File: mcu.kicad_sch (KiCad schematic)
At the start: 25 parts, among them J2 Conn_01x06_GH1.25, SW1 RST, U5 XC6206PxxxMR, U7 AT32F425K8U7-4, U8 TJA1044GTK/3Z, Y1 16MHz

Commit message: 暂存: 基本完成原理图(未分配封装，未ERC)
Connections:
- net CANH: no longer U8.7 (CANH)
- net CANL: no longer U8.6 (CANL)
- net CANH_IN: now reaches D10.1, R11.2, R9.1
- net CANH_IN: now also U8.7 (CANH)
- net CANL_IN: now reaches D10.2, R10.2, R12.2
- net CANL_IN: now also U8.6 (CANL)
- net 5V0 renamed 5V0_{assist}
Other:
- note removed: "差CAN接头"
- moved on the sheet: C60, D10, J2, R10, R11, R12, R9, U7, U8

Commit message: 暂存: 基本完成原理图(差雷达接口)
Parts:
- C1: renamed from C23; footprint Capacitor_SMD:C_0603_1608Metric -> Capacitor_SMD:C_0402_1005Metric
- C11: renamed from C60; footprint (none) -> Capacitor_SMD:C_0402_1005Metric
- C8: renamed from C30; footprint Capacitor_SMD:C_0603_1608Metric -> Capacitor_SMD:C_0402_1005Metric
- R3: renamed from R11; footprint (none) -> Resistor_SMD:R_0402_1005Metric
- R4: renamed from R12; footprint (none) -> Resistor_SMD:R_0402_1005Metric
- R5: renamed from R9; footprint (none) -> Resistor_SMD:R_0402_1005Metric
- R6: renamed from R10; footprint (none) -> Resistor_SMD:R_0402_1005Metric
- renumbered C32 to C10, C24 to C2, C25 to C3, C26 to C4, C27 to C5, C28 to C6, C29 to C7, C31 to C9, D10 to D1, J2 to J1, R15 to R1, R16 to R2, TP3 to TP1, U5 to U1, U7 to U2, U8 to U3
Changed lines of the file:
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@@
 		(dnp no)
 		(fields_autoplaced yes)
-		(property "Reference" "R9"
+		(property "Reference" "R5"
 			(at 161.29 59.6899 0)
 			(effects
@@
 			)
 		)
-		(property "Footprint" ""
+		(property "Footprint" "Resistor_SMD:R_0402_1005Metric"
 			(at 158.75 60.96 0)
 			(effects
@@
 			(project ""
 				(path "/c658c753-a869-4eb9-a520-6b2e7fae7fd9/bed308e1-7b03-4f89-9efc-3e92ee91bd02"
-					(reference "R9")
+					(reference "R5")
 					(unit 1)
 				)
@@
 		(dnp no)
 		(fields_autoplaced yes)
-		(property "Reference" "U7"
+		(property "Reference" "U2"
 			(at 106.68 66.04 0)
 			(effects
@@
 			(project ""
 				(path "/c658c753-a869-4eb9-a520-6b2e7fae7fd9/bed308e1-7b03-4f89-9efc-3e92ee91bd02"
-					(reference "U7")
+					(reference "U2")
 					(unit 1)
 				)
@@
 		(dnp no)
 		(fields_autoplaced yes)
-		(property "Reference" "#PWR6"
+		(property "Reference" "#PWR1"
 			(at 172.72 81.28 0)
 			(effects
@@
 			(project ""
 				(path "/c658c753-a869-4eb9-a520-6b2e7fae7fd9/bed308e1-7b03-4f89-9efc-3e92ee91bd02"
-					(reference "#PWR6")
+					(reference "#PWR1")
 					(unit 1)
 				)
@@
 		(on_board yes)
 		(dnp no)
-		(property "Reference" "TP3"
+		(property "Reference" "TP1"
 			(at 75.184 30.988 0)
 			(effects
@@
 			(project "ZW1S"
 				(path "/c658c753-a869-4eb9-a520-6b2e7fae7fd9/bed308e1-7b03-4f89-9efc-3e92ee91bd02"
-					(reference "TP3")
+					(reference "TP1")
 					(unit 1)
 				)
@@
 		(dnp no)
 		(fields_autoplaced yes)
-		(property "Reference" "C23"
+		(property "Reference" "C1"
 			(at 40.64 36.8362 0)
 			(effects
@@
 			)
 		)
-		(property "Footprint" "Capacitor_SMD:C_0603_1608Metric"
+		(property "Footprint" "Capacitor_SMD:C_0402_1005Metric"
 			(at 38.1 38.1 0)
 			(effects
@@
 			(project "ZW1S"
 				(path "/c658c753-a869-4eb9-a520-6b2e7fae7fd9/bed308e1-7b03-4f89-9efc-3e92ee91bd02"
-					(reference "C23")
+					(reference "C1")
 					(unit 1)
 				)
@@
 		(dnp no)
 		(fields_autoplaced yes)
-		(property "Reference" "R12"
+		(property "Reference" "R4"
 			(at 153.67 67.31 90)
 			(effects
@@
 			)
 		)
-		(property "Footprint" ""
+		(property "Footprint" "Resistor_SMD:R_0402_1005Metric"
 			(at 153.67 72.39 0)
 			(effects
@@
 			(project "ZW1S"
 				(path "/c658c753-a869-4eb9-a520-6b2e7fae7fd9/bed308e1-7b03-4f89-9efc-3e92ee91bd02"
-					(reference "R12")
+					(reference "R4")
 					(unit 1)
 				)
@@
 		(on_board yes)
 		(dnp no)
-		(property "Reference" "C25"
+		(property "Reference" "C3"
 			(at 39.37 120.65 90)
 			(effects
@@
 			(project "ZW1S"
 				(path "/c658c753-a869-4eb9-a520-6b2e7fae7fd9/bed308e1-7b03-4f89-9efc-3e92ee91bd02"
-					(reference "C25")
+					(reference "C3")
 					(unit 1)
 				)
@@
 		(on_board yes)
 		(dnp no)
-		(property "Reference" "R16"
+		(property "Reference" "R2"
 			(at 40.132 59.69 90)
 			(effects
@@
 			(project "ZW1S"
 				(path "/c658c753-a869-4eb9-a520-6b2e7fae7fd9/bed308e1-7b03-4f89-9efc-3e92ee91bd02"
-					(reference "R16")
+					(reference "R2")
 					(unit 1)
 				)
@@
 		(on_board yes)
 		(dnp no)
-		(property "Reference" "C28"
+		(property "Reference" "C6"
 			(at 38.1 134.62 90)
 			(effects
@@
 			(project "ZW1S"
 				(path "/c658c753-a869-4eb9-a520-6b2e7fae7fd9/bed308e1-7b03-4f89-9efc-3e92ee91bd02"
-					(reference "C28")
+					(reference "C6")
 					(unit 1)
 				)
@@
 		(dnp no)
 		(fields_autoplaced yes)
-		(property "Reference" "D10"
+		(property "Reference" "D1"
 			(at 181.61 55.88 0)
 			(effects
@@
 			(project ""
 				(path "/c658c753-a869-4eb9-a520-6b2e7fae7fd9/bed308e1-7b03-4f89-9efc-3e92ee91bd02"
-					(reference "D10")
+					(reference "D1")
 					(unit 1)
 				)
@@
 		(on_board yes)
 		(dnp no)
-		(property "Reference" "C27"
+		(property "Reference" "C5"
 			(at 38.1 130.81 90)
 			(effects
@@
 			(project "ZW1S"
 				(path "/c658c753-a869-4eb9-a520-6b2e7fae7fd9/bed308e1-7b03-4f89-9efc-3e92ee91bd02"
-					(reference "C27")
+					(reference "C5")
 					(unit 1)
 				)
@@
 		(on_board yes)
 		(dnp no)
-		(property "Reference" "J2"
+		(property "Reference" "J1"
 			(at 153.924 113.538 0)
 			(effects
@@
 			(project "ZW1S"
 				(path "/c658c753-a869-4eb9-a520-6b2e7fae7fd9/bed308e1-7b03-4f89-9efc-3e92ee91bd02"
-					(reference "J2")
+					(reference "J1")
 					(unit 1)
 				)
@@
 		(on_board yes)
 		(dnp yes)
-		(property "Reference" "C60"
+		(property "Reference" "C11"
 			(at 167.894 61.722 90)
 			(effects
@@
 			)
 		)
-		(property "Footprint" ""
+		(property "Footprint" "Capacitor_SMD:C_0402_1005Metric"
 			(at 168.91 64.77 0)
 			(effects
@@
 			(project ""
 				(path "/c658c753-a869-4eb9-a520-6b2e7fae7fd9/bed308e1-7b03-4f89-9efc-3e92ee91bd02"
-					(reference "C60")
+					(reference "C11")
 					(unit 1)
 				)
@@
 		(on_board yes)
 		(dnp no)
-		(property "Reference" "C30"
+		(property "Reference" "C8"
 			(at 67.31 36.8362 0)
 			(effects
@@
 			)
 		)
-		(property "Footprint" "Capacitor_SMD:C_0603_1608Metric"
+		(property "Footprint" "Capacitor_SMD:C_0402_1005Metric"
 			(at 69.85 38.1 0)
 			(effects
@@
 			(project "ZW1S"
 				(path "/c658c753-a869-4eb9-a520-6b2e7fae7fd9/bed308e1-7b03-4f89-9efc-3e92ee91bd02"
-					(reference "C30")
+					(reference "C8")
 					(unit 1)
 				)
@@
 		(on_board yes)
 		(dnp no)
-		(property "Reference" "U5"
+		(property "Reference" "U1"
 			(at 44.958 29.21 0)
 			(effects
@@
 			(project "ZW1S"
 				(path "/c658c753-a869-4eb9-a520-6b2e7fae7fd9/bed308e1-7b03-4f89-9efc-3e92ee91bd02"
-					(reference "U5")
+					(reference "U1")
 					(unit 1)
 				)
@@
 		(on_board yes)
 		(dnp yes)
-		(property "Reference" "R15"
+		(property "Reference" "R1"
 			(at 40.132 53.34 90)
 			(effects
@@
 			(project "ZW1S"
 				(path "/c658c753-a869-4eb9-a520-6b2e7fae7fd9/bed308e1-7b03-4f89-9efc-3e92ee91bd02"
-					(reference "R15")
+					(reference "R1")
 					(unit 1)
 				)
@@
 		(dnp no)
 		(fields_autoplaced yes)
-		(property "Reference" "C31"
+		(property "Reference" "C9"
 			(at 104.1463 27.94 90)
 			(effects
@@
 			(project "ZW1S"
 				(path "/c658c753-a869-4eb9-a520-6b2e7fae7fd9/bed308e1-7b03-4f89-9efc-3e92ee91bd02"
-					(reference "C31")
+					(reference "C9")
 					(unit 1)
 				)
@@
 		(dnp no)
 		(fields_autoplaced yes)
-		(property "Reference" "C32"
+		(property "Reference" "C10"
 			(at 104.1463 33.02 90)
 			(effects
@@
 			(project "ZW1S"
 				(path "/c658c753-a869-4eb9-a520-6b2e7fae7fd9/bed308e1-7b03-4f89-9efc-3e92ee91bd02"
-					(reference "C32")
+					(reference "C10")
 					(unit 1)
 				)
@@
 		(dnp no)
 		(fields_autoplaced yes)
-		(property "Reference" "C29"
+		(property "Reference" "C7"
 			(at 46.99 78.1113 0)
 			(effects
@@
 			(project "ZW1S"
 				(path "/c658c753-a869-4eb9-a520-6b2e7fae7fd9/bed308e1-7b03-4f89-9efc-3e92ee91bd02"
-					(reference "C29")
+					(reference "C7")
 					(unit 1)
 				)
@@
 		(on_board yes)
 		(dnp no)
-		(property "Reference" "C24"
+		(property "Reference" "C2"
 			(at 38.1 113.03 90)
 			(effects
@@
 			(project "ZW1S"
 				(path "/c658c753-a869-4eb9-a520-6b2e7fae7fd9/bed308e1-7b03-4f89-9efc-3e92ee91bd02"
-					(reference "C24")
+					(reference "C2")
 					(unit 1)
 				)
@@
 		(dnp no)
 		(fields_autoplaced yes)
-		(property "Reference" "U8"
+		(property "Reference" "U3"
 			(at 166.37 27.94 0)
 			(effects
@@
 			(project ""
 				(path "/c658c753-a869-4eb9-a520-6b2e7fae7fd9/bed308e1-7b03-4f89-9efc-3e92ee91bd02"
-					(reference "U8")
+					(reference "U3")
 					(unit 1)
 				)
@@
 		(dnp no)
 		(fields_autoplaced yes)
-		(property "Reference" "R10"
+		(property "Reference" "R6"
 			(at 161.29 67.3099 0)
 			(effects
@@
 			)
 		)
-		(property "Footprint" ""
+		(property "Footprint" "Resistor_SMD:R_0402_1005Metric"
 			(at 158.75 68.58 0)
 			(effects
@@
 			(project "ZW1S"
 				(path "/c658c753-a869-4eb9-a520-6b2e7fae7fd9/bed308e1-7b03-4f89-9efc-3e92ee91bd02"
-					(reference "R10")
+					(reference "R6")
 					(unit 1)
 				)
@@
 		(on_board yes)
 		(dnp no)
-		(property "Reference" "C26"
+		(property "Reference" "C4"
 			(at 38.1 127 90)
 			(effects
@@
 			(project "ZW1S"
 				(path "/c658c753-a869-4eb9-a520-6b2e7fae7fd9/bed308e1-7b03-4f89-9efc-3e92ee91bd02"
-					(reference "C26")
+					(reference "C4")
 					(unit 1)
 				)
@@
 		(dnp no)
 		(fields_autoplaced yes)
-		(property "Reference" "R11"
+		(property "Reference" "R3"
 			(at 153.67 52.07 90)
 			(effects
@@
 			)
 		)
-		(property "Footprint" ""
+		(property "Footprint" "Resistor_SMD:R_0402_1005Metric"
 			(at 153.67 57.15 0)
 			(effects
@@
 			(project "ZW1S"
 				(path "/c658c753-a869-4eb9-a520-6b2e7fae7fd9/bed308e1-7b03-4f89-9efc-3e92ee91bd02"
-					(reference "R11")
-					(unit 1)
-				)
+					(reference "R3")
+					(unit 1)
+				)

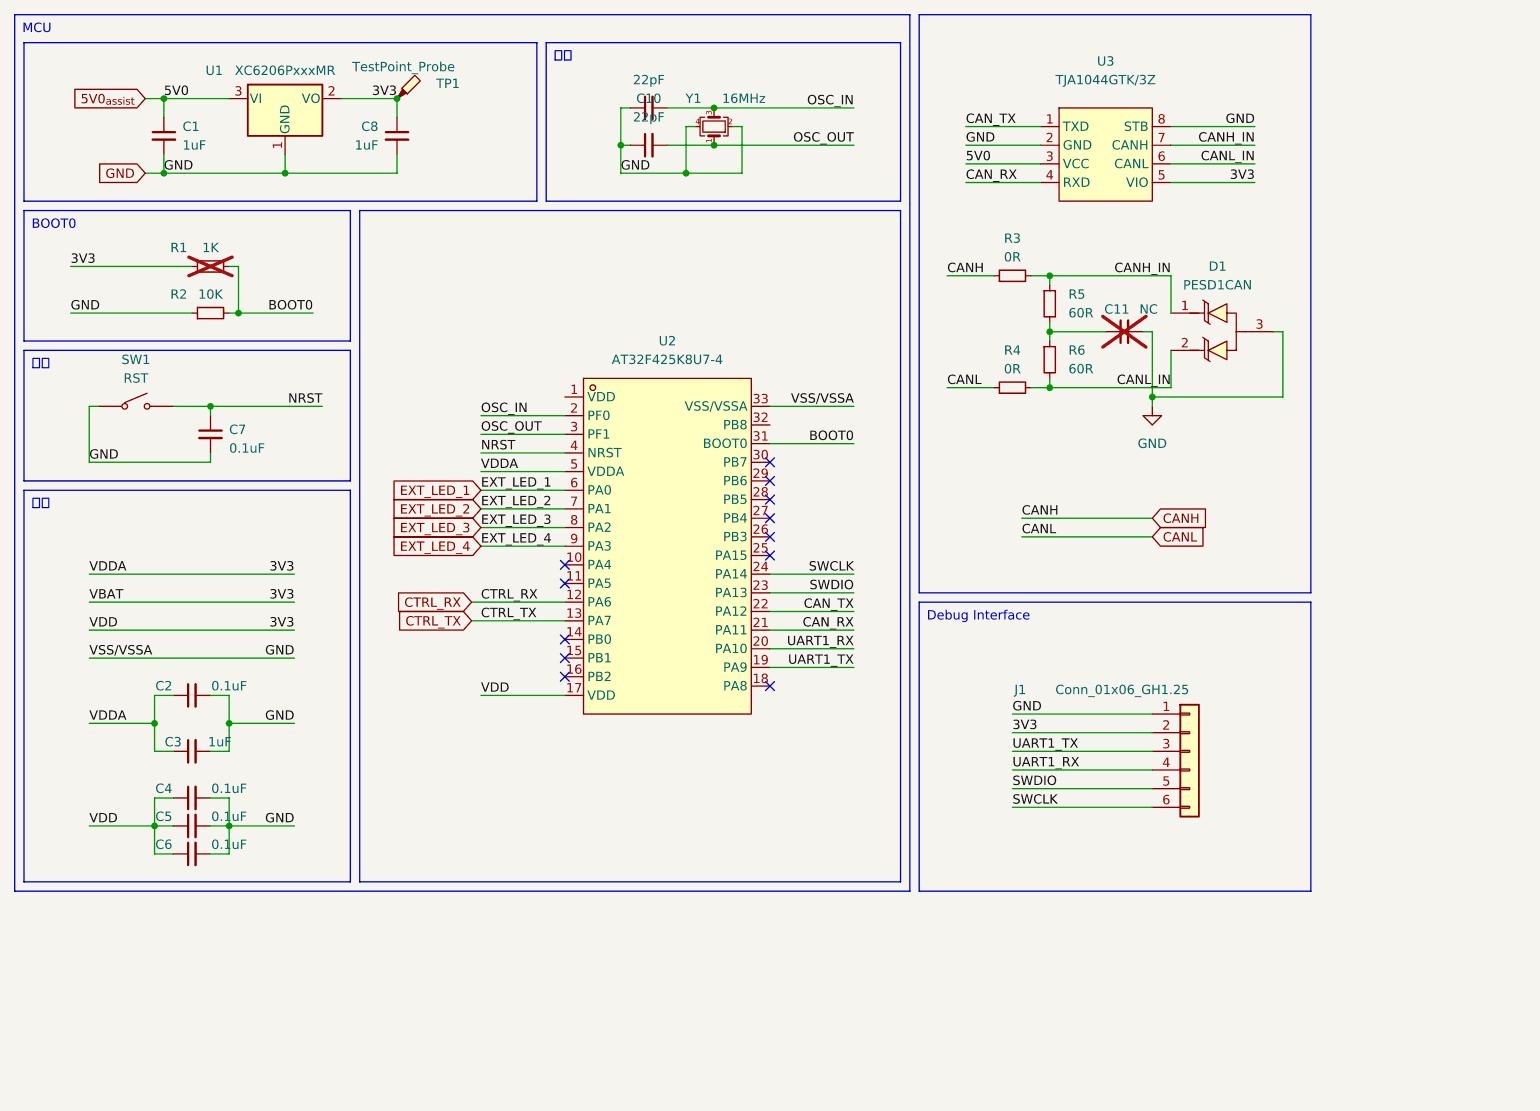
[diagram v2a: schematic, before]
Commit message: 暂存: 布局布线基本完成(DRC未过，GND不全)
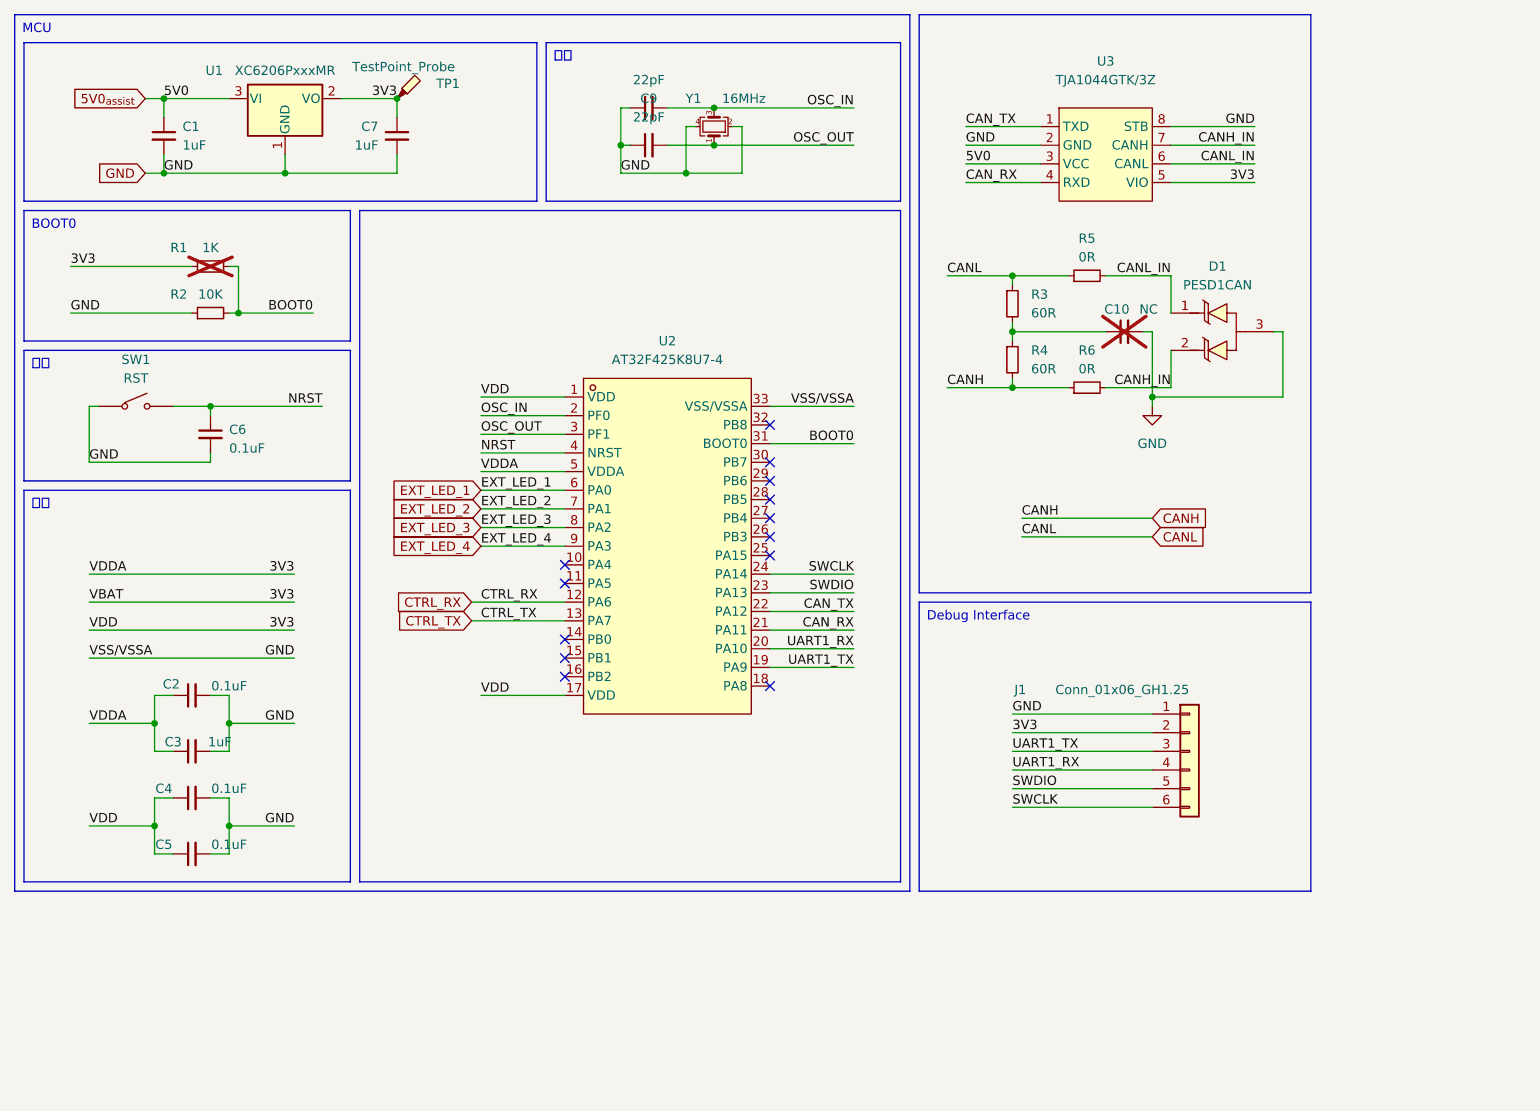
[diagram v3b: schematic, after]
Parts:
- removed C5: 0.1uF, Capacitor_SMD:C_0402_1005Metric, symbol Device:C_Small
- renumbered C11 to C10, C6 to C5, C7 to C6, C8 to C7, C9 to C8, C10 to C9, R5 to R3, R6 to R4, R3 to R5, R4 to R6
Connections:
- net 3V3: now also U2.1 (VDD)
- net CANH: now also R4.2, R6.1; no longer R5.1
- net CANH_IN: now also D1.2, R6.2; no longer D1.1, R3.1, R5.2
- net CANL: now also R3.1, R5.1; no longer R6.1
- net CANL_IN: now also D1.1, R5.2; no longer D1.2, R4.2, R6.2
- no-connect marks 12 -> 13
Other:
- moved on the sheet: R3, R4, R5, R6

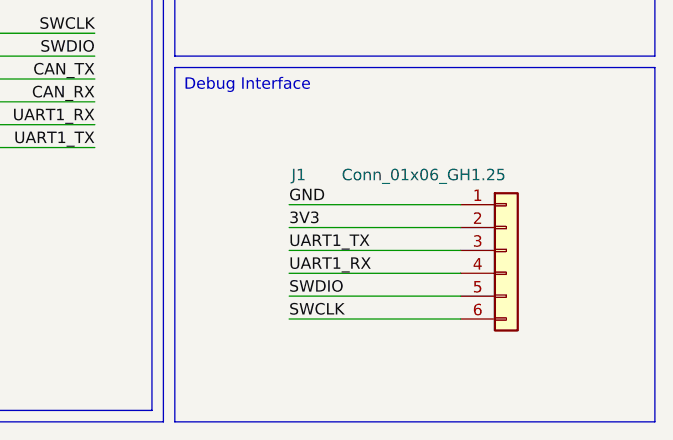
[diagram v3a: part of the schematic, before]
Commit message: pref: USB外设改自供电，优化布线
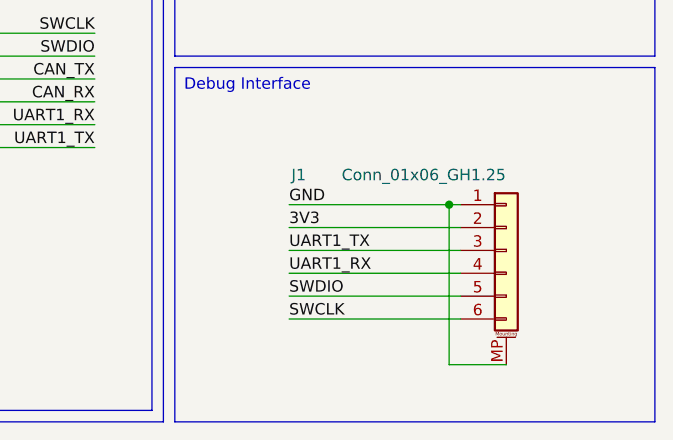
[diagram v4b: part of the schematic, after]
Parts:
- J1: footprint Connector_JST:JST_GH_BM06B-GHS-TBT_1x06-1MP_P1.25mm_Vertical -> Connector_JST:JST_GH_SM06B-GHS-TB_1x06-1MP_P1.25mm_Horizontal; symbol Connector_Generic:Conn_01x06 -> Connector_Generic_MountingPin:Conn_01x06_MountingPin
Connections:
- net EP: now also J1.MP (MountPin)
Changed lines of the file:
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@@
+		(color 0 0 0 0)
+	)
+	(junction
+		(at 171.45 116.84)
+		(diameter 0)
 		(color 0 0 0 0)
 	)
@@
 	(wire
 		(pts
+			(xy 171.45 116.84) (xy 172.72 116.84)
+		)
+		(stroke
+			(width 0)
+			(type default)
+		)
+	)
+	(wire
+		(pts
 			(xy 154.94 90.17) (xy 172.72 90.17)
 		)
@@
 	(wire
 		(pts
+			(xy 177.8 134.62) (xy 171.45 134.62)
+		)
+		(stroke
+			(width 0)
+			(type default)
+		)
+	)
+	(wire
+		(pts
 			(xy 175.26 62.23) (xy 175.26 57.15)
 		)
@@
 	(wire
 		(pts
+			(xy 171.45 134.62) (xy 171.45 116.84)
+		)
+		(stroke
+			(width 0)
+			(type default)
+		)
+	)
+	(wire
+		(pts
 			(xy 81.28 88.9) (xy 92.71 88.9)
 		)
@@
 	(wire
 		(pts
-			(xy 153.67 116.84) (xy 172.72 116.84)
+			(xy 153.67 116.84) (xy 171.45 116.84)
 		)
 		(stroke
@@
 	)
 	(symbol
-		(lib_id "Connector_Generic:Conn_01x06")
+		(lib_id "Connector_Generic_MountingPin:Conn_01x06_MountingPin")
 		(at 177.8 121.92 0)
 		(unit 1)
@@
 			)
 		)
-		(property "Footprint" "Connector_JST:JST_GH_BM06B-GHS-TBT_1x06-1MP_P1.25mm_Vertical"
+		(property "Footprint" "Connector_JST:JST_GH_SM06B-GHS-TB_1x06-1MP_P1.25mm_Horizontal"
 			(at 177.8 121.92 0)
 			(effects
@@
 			)
 		)
-		(property "Description" "Generic connector, single row, 01x06, script generated (kicad-library-utils/schlib/autogen/connector/)"
+		(property "Description" "Generic connectable mounting pin connector, single row, 01x06, script generated (kicad-library-utils/schlib/autogen/connector/)"
 			(at 177.8 121.92 0)
 			(effects
@@
 		(pin "4"
 		)
+		(pin "MP"
+		)
 		(instances
